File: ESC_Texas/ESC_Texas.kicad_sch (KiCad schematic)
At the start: 27 parts, among them IC2 nRF52840-QFAA-F-R7, J1 Conn_01x03_Pin, J2 Conn_01x10_Pin, J3 Conn_01x10_Pin, J4 Conn_01x05_Pin, J5 Conn_01x10_Pin, Y1 32MHz, Y2 32.768kHz

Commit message: Started PCB layouting
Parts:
- J4: footprint Connector_PinSocket_2.54mm:PinSocket_1x05_P2.54mm_Horizontal -> Connector_PinHeader_2.54mm:PinHeader_1x05_P2.54mm_Vertical
- J5: footprint Connector_PinSocket_2.54mm:PinSocket_1x10_P2.54mm_Vertical -> Connector_PinHeader_2.54mm:PinHeader_1x10_P2.54mm_Vertical
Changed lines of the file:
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@@
 	)
 	(no_connect
-		(at 49.53 45.72)
+		(at 48.26 45.72)
 	)
 	(no_connect
@@
 			)
 		)
-		(property "Footprint" "Connector_PinSocket_2.54mm:PinSocket_1x05_P2.54mm_Horizontal"
+		(property "Footprint" "Connector_PinHeader_2.54mm:PinHeader_1x05_P2.54mm_Vertical"
 			(at 158.75 125.73 0)
 			(effects
@@
 			)
 		)
-		(property "Footprint" "Connector_PinSocket_2.54mm:PinSocket_1x10_P2.54mm_Vertical"
+		(property "Footprint" "Connector_PinHeader_2.54mm:PinHeader_1x10_P2.54mm_Vertical"
 			(at 43.18 33.02 0)
 			(effects

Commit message: Layout done
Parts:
- removed C14: 1.2pF, Capacitor_SMD:C_0805_2012Metric, symbol Device:C
- removed J1: Conn_01x03_Pin, Connector_PinHeader_2.54mm:PinHeader_1x03_P2.54mm_Vertical, symbol Connector:Conn_01x03_Pin
- removed J3, J5: Conn_01x10_Pin, Connector_PinHeader_2.54mm:PinHeader_1x10_P2.54mm_Vertical, symbol Connector:Conn_01x10_Pin
- removed L3: 4.7nH, Inductor_SMD:L_1008_2520Metric_Pad1.43x2.20mm_HandSolder, symbol Device:L
- removed L4: 2.2nH, Inductor_SMD:L_1008_2520Metric_Pad1.43x2.20mm_HandSolder, symbol Device:L
- removed Y1: 32MHz, symbol Device:Crystal
- removed Y2: 32.768kHz, symbol Device:Crystal
- added J11: Conn_01x01_Pin, Connector_PinHeader_2.54mm:PinHeader_1x01_P2.54mm_Vertical, symbol Connector:Conn_01x01_Pin
- added J12, J2: Conn_01x05_Pin, Connector_PinHeader_2.54mm:PinHeader_1x05_P2.54mm_Vertical, symbol Connector:Conn_01x05_Pin
- added PS1: MP-K78U15-500R3L, MP-K78U15-500R3L:MPK78U15500R3L, symbol MP-K78U15-500R3L:MP-K78U15-500R3L
- added Y1: CM7V-T1A-32.768kHz, CM7V-T1A-32.768KHZ-12.5PF-20PPM-TA-QC:CM7V32768TBQA020, symbol CM7V-T1A-32.768KHZ-12.5PF-20PP:CM7V-T1A-32.768KHZ-12.5PF-20PPM-TA-QC
- added Y2: 32MHz, XRCGB32M000F2P29R0:XRCGB, symbol XRCGB32M000F2P29R0:XRCGB32M000F2P29R0
- renumbered C15 to C12, C12 to C13, C13 to C14, IC2 to IC1, J2 to J1
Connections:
- net ANT: no longer C11.2, IC1.32 (VSS_PA)
- net GND: now also PS1.2 (GND)
- net P0.02: now also J2.2 (Pin_2)
- net P0.13: now also J12.4 (Pin_4)
- net P0.28: now also J2.1 (Pin_1)
- net P1.00: now also J11.1 (Pin_1)
- net P1.14: now also J12.3 (Pin_3)
- net P1.15: now also J2.4 (Pin_4)
- net P1.17: now also J12.2 (Pin_2)
- net P1.18: now also J12.1 (Pin_1)
- net Po.03: now also J2.3 (Pin_3)
- net XC1: now also Y2.3 (XTAL_2)
- net XC2: now also Y2.1 (XTAL_1)
- net at C1.2, IC1.2 (P0.00/XL1): now also Y1.2
- net at C2.2, IC1.3 (P0.01/XL2): now also Y1.1
- new net +15V: PS1.3 (+VO)
- new net +36V: PS1.1 (VIN)
- new net VSS_PA: C11.2, IC1.32 (VSS_PA)
- no-connect marks 11 -> 7
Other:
- removed sheet Driver_subsheet_1
- added sheet Phase1 (Phase_subsheet.kicad_sch)
- added sheet Phase2 (Phase_subsheet.kicad_sch)
- added sheet Phase3 (Phase_subsheet.kicad_sch)
- moved on the sheet: C1, C10, C11, C12, C13, C14, C2, C3, C4, C5, C6, C7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

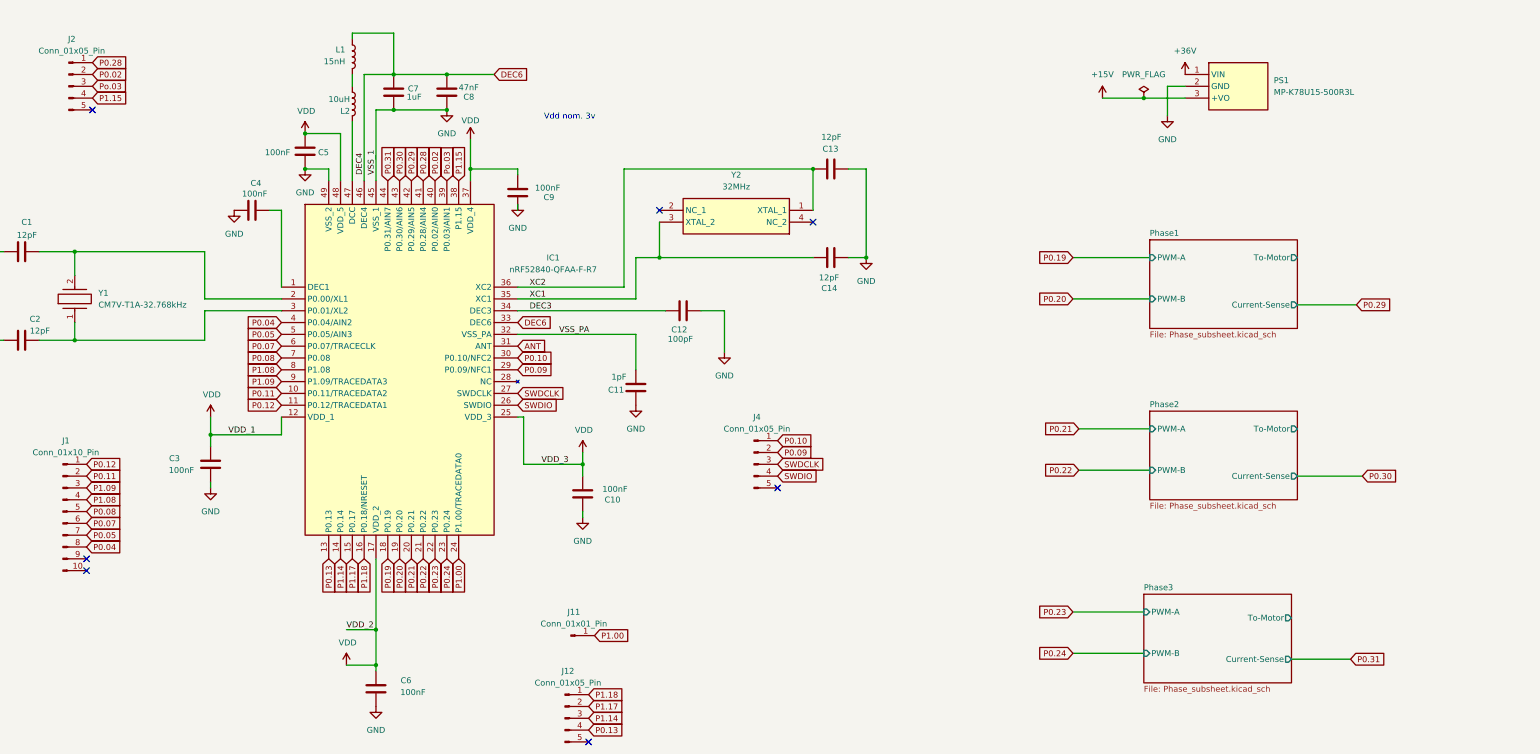
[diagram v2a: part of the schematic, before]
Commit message: Added bypass capacitors to dc/dc...
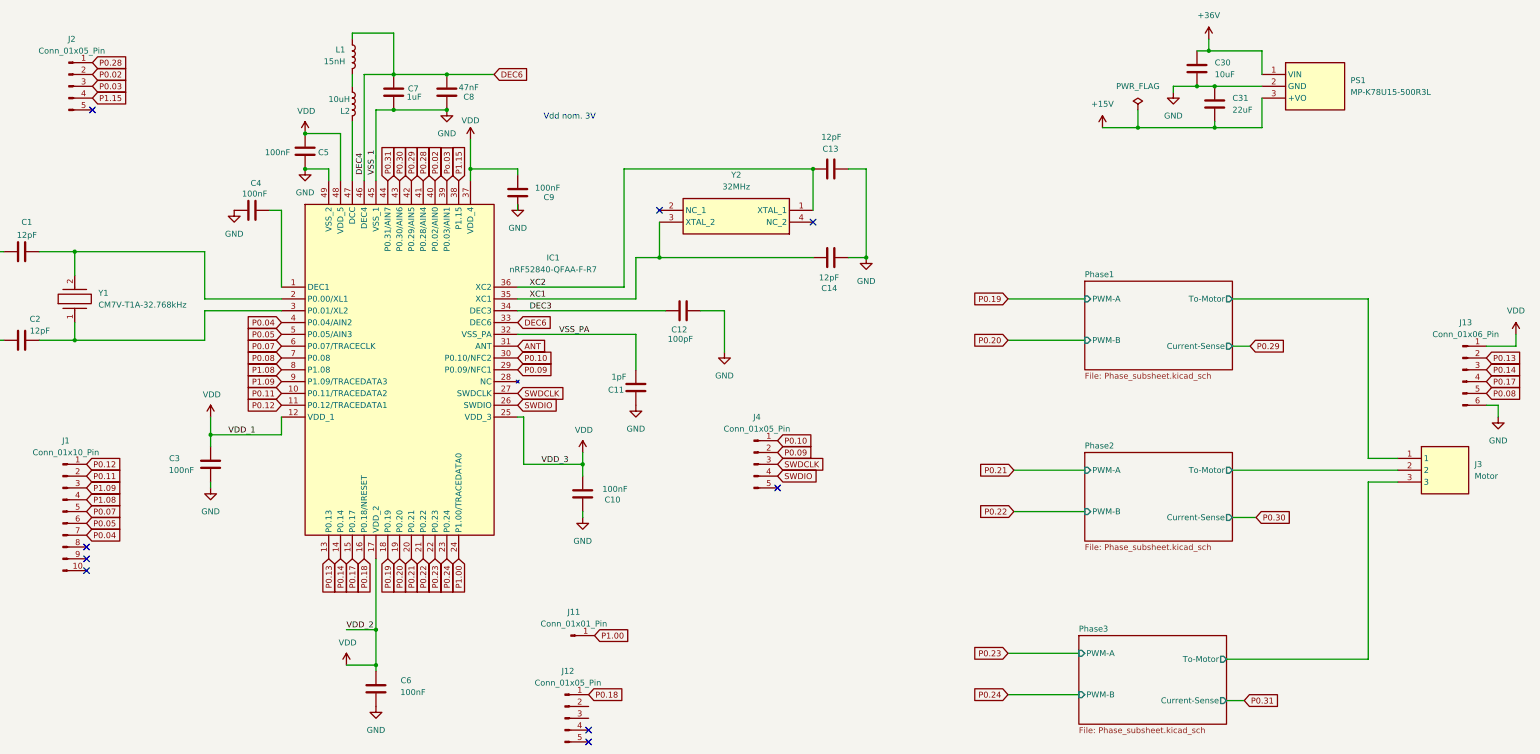
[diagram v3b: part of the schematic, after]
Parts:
- added C30: 10uF, symbol Device:C
- added C31: 22uF, symbol Device:C
- added J13: Conn_01x06_Pin, symbol Connector:Conn_01x06_Pin
- added J3: Motor, SHDRRA3W90P0X350_1X3_1110X920X691P, symbol 2350514-3:2350514-3
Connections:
- net +15V: now also C31.2
- net +36V: now also C30.1
- net GND: now also C30.2, C31.1, J13.6 (Pin_6)
- net P0.04: now also J1.7 (Pin_7); no longer J1.8 (Pin_8)
- net P0.05: now also J1.6 (Pin_6); no longer J1.7 (Pin_7)
- net P0.07: now also J1.5 (Pin_5); no longer J1.6 (Pin_6)
- net P0.08: now also J13.5 (Pin_5); no longer J1.5 (Pin_5)
- net P0.13: now also J13.2 (Pin_2); no longer J12.4 (Pin_4)
- net Phase1/To-Motor: now also J3.1
- net Phase2/To-Motor: now also J3.2
- net Phase3/To-Motor: now also J3.3
- net Po.03: no longer J2.3 (Pin_3)
- net VDD: now also J13.1 (Pin_1)
- net P1.14: no longer names the net of J12.3 (Pin_3)
- net P1.14: no longer IC1.14 (P0.14)
- net P1.17: no longer names the net of J12.2 (Pin_2)
- net P1.17: no longer IC1.15 (P0.17)
- net P1.18 renamed P0.18
- new net P0.03: J2.3 (Pin_3)
- new net P0.14: IC1.14 (P0.14), J13.3 (Pin_3)
- new net P0.17: IC1.15 (P0.17), J13.4 (Pin_4)
- no-connect marks 7 -> 9
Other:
- note added: "Vdd nom. 3V"
- note removed: "Vdd nom. 3v"
- moved on the sheet: PS1

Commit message: More routing done
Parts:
- removed J11: Conn_01x01_Pin, Connector_PinHeader_2.54mm:PinHeader_1x01_P2.54mm_Vertical, symbol Connector:Conn_01x01_Pin
- added C33, C34: 0.1uF, Capacitor_SMD:C_0805_2012Metric, symbol Device:C
- added IC11: LM3480IM3-3.3_NOPB, LM3480IM3-3.3_NOPB:SOT95P237X112-3N, symbol LM3480IM3-3_3_NOPB:LM3480IM3-3.3_NOPB
- C30, C31: footprint (none) -> Capacitor_SMD:C_0805_2012Metric
- J13: footprint (none) -> Connector_PinHeader_2.54mm:PinHeader_1x06_P2.54mm_Vertical
- J3: footprint SHDRRA3W90P0X350_1X3_1110X920X691P -> LIB_2350514-3:SHDRRA3W90P0X350_1X3_1110X920X691P
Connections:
- net +15V: now also C34.1, IC11.2 (IN)
- net GND: now also C33.2, C34.2, IC11.3 (GND)
- net P0.13: now also J13.4 (Pin_4); no longer J13.2 (Pin_2)
- net P0.17: now also J13.2 (Pin_2); no longer J13.4 (Pin_4)
- net P0.18: now also J12.2 (Pin_2); no longer J12.1 (Pin_1)
- net P1.00: now also J12.1 (Pin_1)
- net VDD: now also C33.1, IC11.1 (OUT)
- no-connect marks 9 -> 10
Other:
- moved on the sheet: C1, C10, C11, C12, C13, C14, C2, C3, C30, C31, C4, C5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

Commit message: PCB layout done
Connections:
- net Po.03 is gone; now on net P0.03: IC1.39 (P0.03/AIN1)
- net P0.02: now also J2.3 (Pin_3); no longer J2.2 (Pin_2)
- net P0.03: now also J2.4 (Pin_4); no longer J2.3 (Pin_3)
- net P0.28: now also J2.2 (Pin_2); no longer J2.1 (Pin_1)
- net P1.15: now also J2.5 (Pin_5); no longer J2.4 (Pin_4)

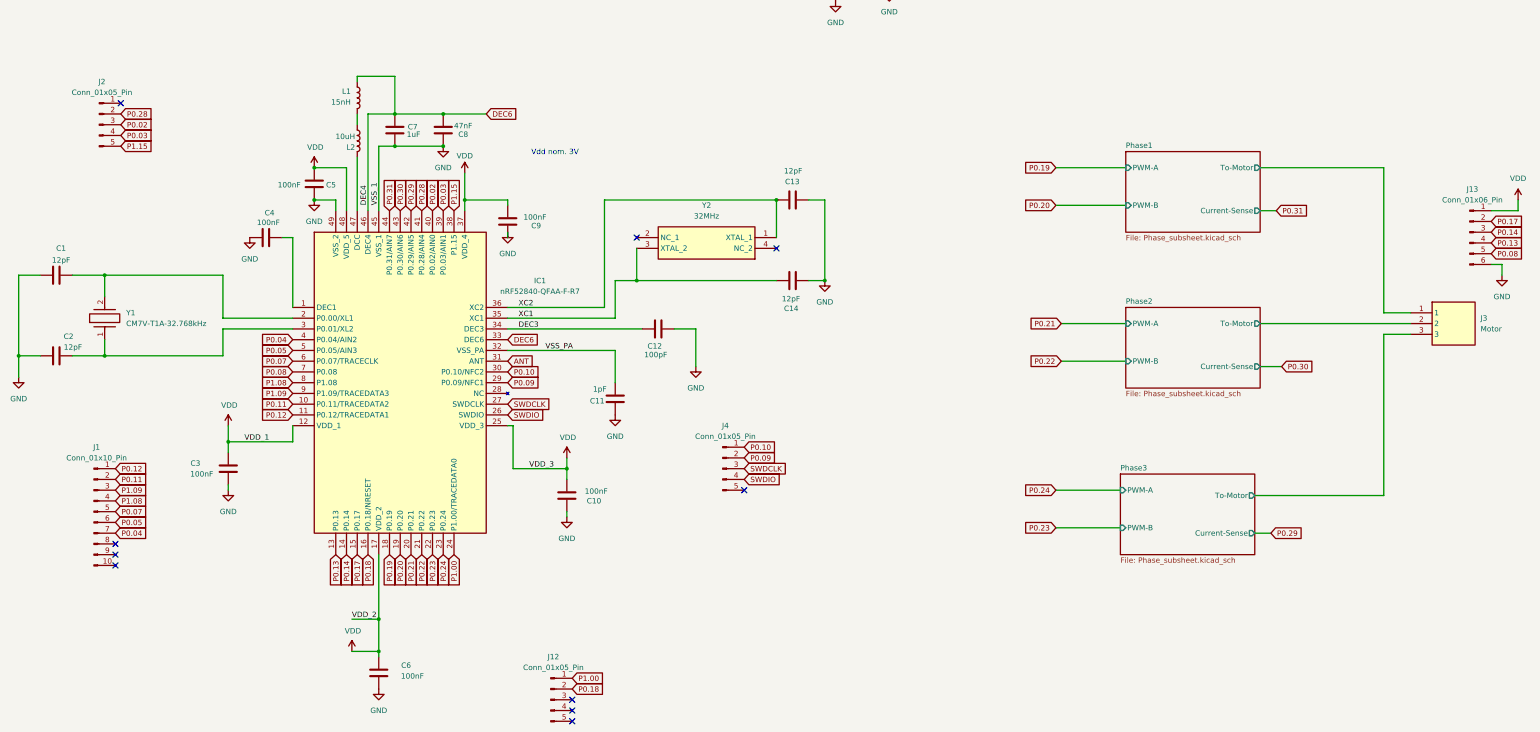
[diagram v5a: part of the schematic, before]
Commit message: Removed excess pin headers
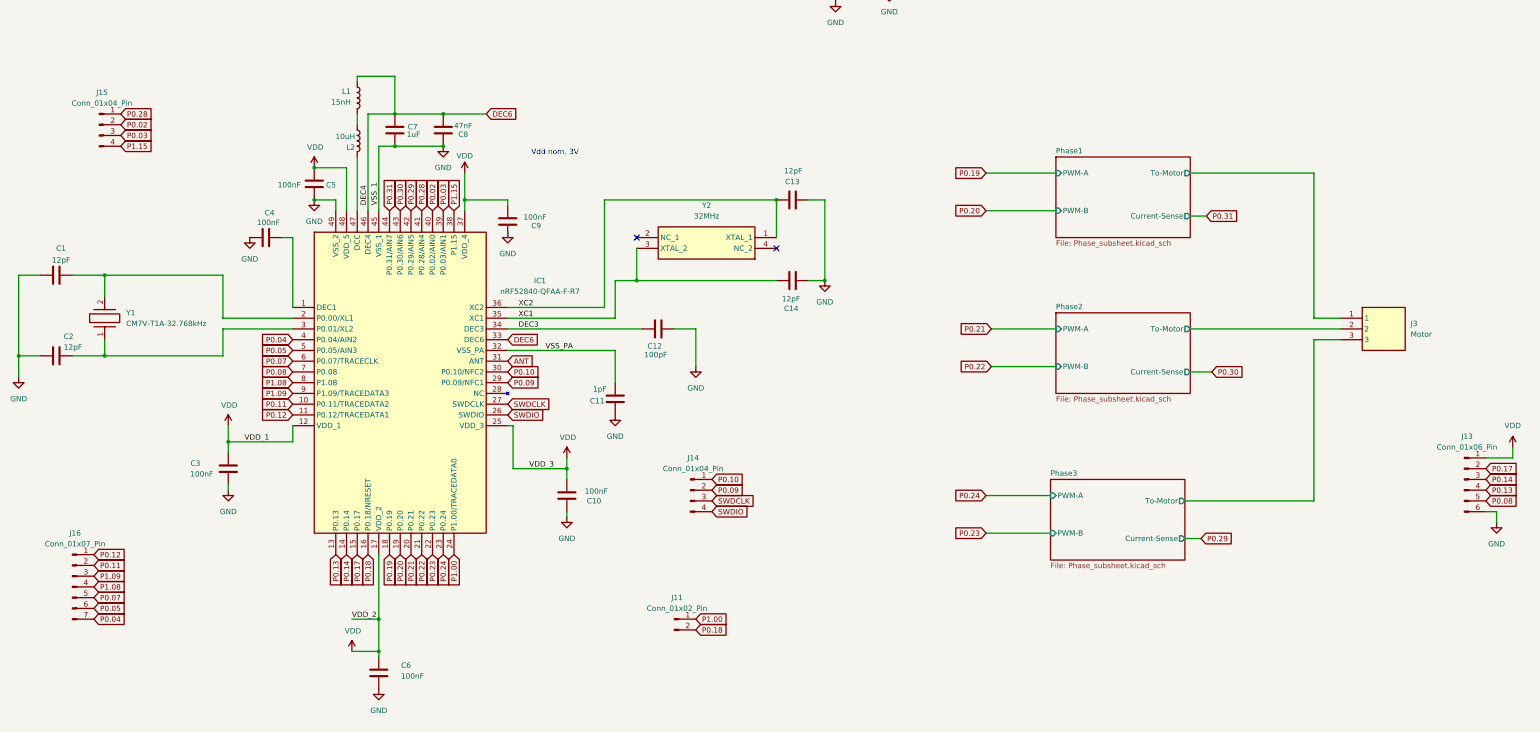
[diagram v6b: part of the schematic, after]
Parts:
- removed J1: Conn_01x10_Pin, Connector_PinHeader_2.54mm:PinHeader_1x10_P2.54mm_Vertical, symbol Connector:Conn_01x10_Pin
- removed J12, J2, J4: Conn_01x05_Pin, Connector_PinHeader_2.54mm:PinHeader_1x05_P2.54mm_Vertical, symbol Connector:Conn_01x05_Pin
- added J11: Conn_01x02_Pin, Connector_PinHeader_2.54mm:PinHeader_1x02_P2.54mm_Vertical, symbol Connector:Conn_01x02_Pin
- added J14, J15: Conn_01x04_Pin, Connector_PinHeader_2.54mm:PinHeader_1x04_P2.54mm_Vertical, symbol Connector:Conn_01x04_Pin
- added J16: Conn_01x07_Pin, Connector_PinHeader_2.54mm:PinHeader_1x07_P2.54mm_Vertical, symbol Connector:Conn_01x07_Pin
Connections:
- net P0.02: now also J15.2 (Pin_2)
- net P0.03: now also J15.3 (Pin_3)
- net P0.04: now also J16.7 (Pin_7)
- net P0.05: now also J16.6 (Pin_6)
- net P0.07: now also J16.5 (Pin_5)
- net P0.09: now also J14.2 (Pin_2)
- net P0.10: now also J14.1 (Pin_1)
- net P0.11: now also J16.2 (Pin_2)
- net P0.12: now also J16.1 (Pin_1)
- net P0.18: now also J11.2 (Pin_2)
- net P0.28: now also J15.1 (Pin_1)
- net P1.00: now also J11.1 (Pin_1)
- net P1.08: now also J16.4 (Pin_4)
- net P1.09: now also J16.3 (Pin_3)
- net P1.15: now also J15.4 (Pin_4)
- net SWDCLK: now also J14.3 (Pin_3)
- net SWDIO: now also J14.4 (Pin_4)
- no-connect marks 10 -> 2
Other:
- moved on the sheet: J13, J3

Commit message: More gnd vias added
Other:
- note added: "15 V regulator"
- note added: "3.3 V regulator"
- note added: "Input/Output to the motor"
- note added: "nRF52840 Circuit"
- moved on the sheet: C30, C31, C33, C34, IC11, J13, J3, PS1

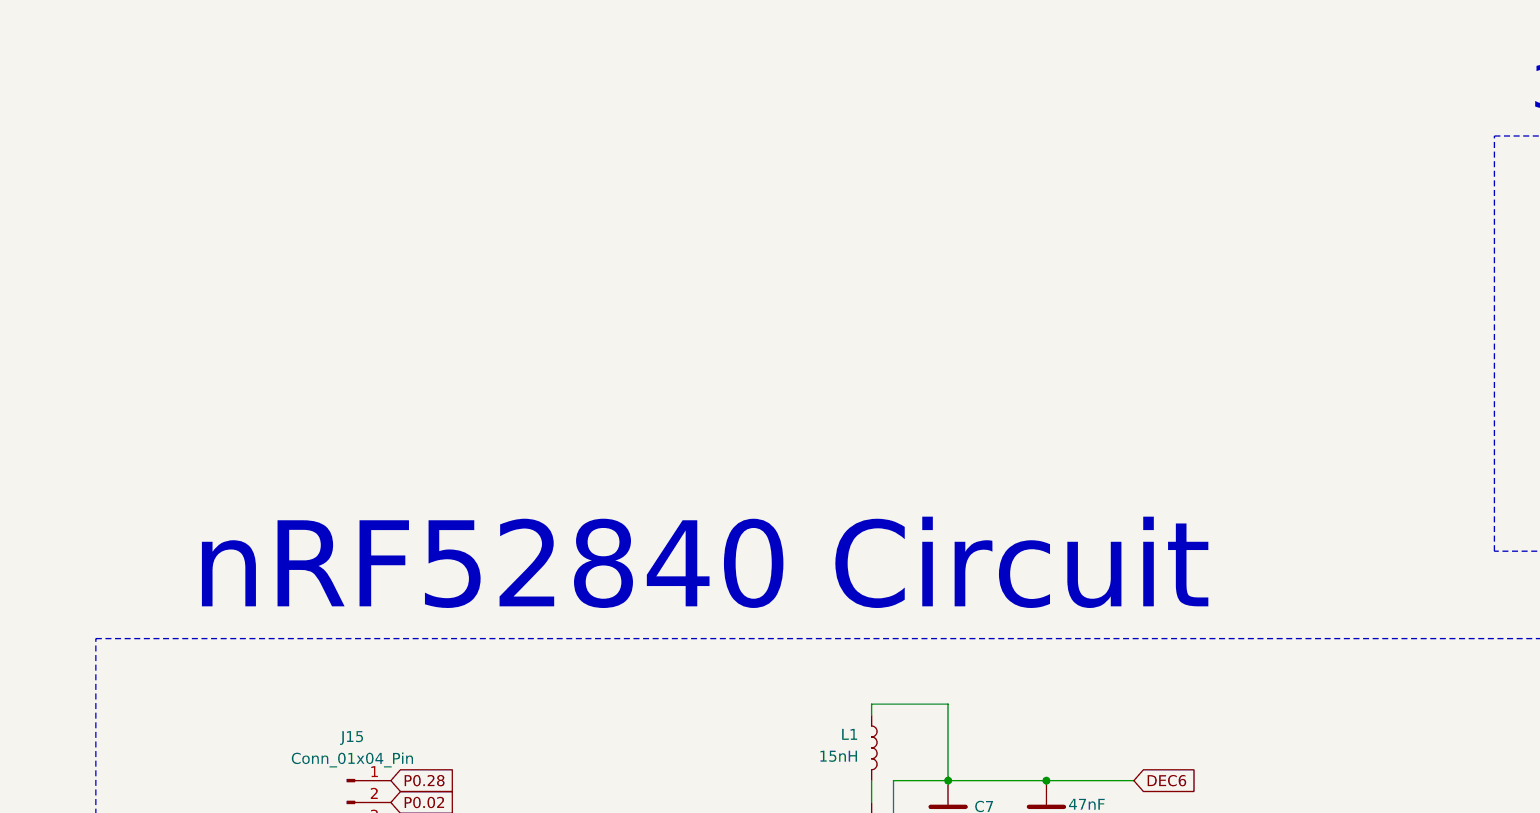
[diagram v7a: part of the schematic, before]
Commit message: Added capacitors and more
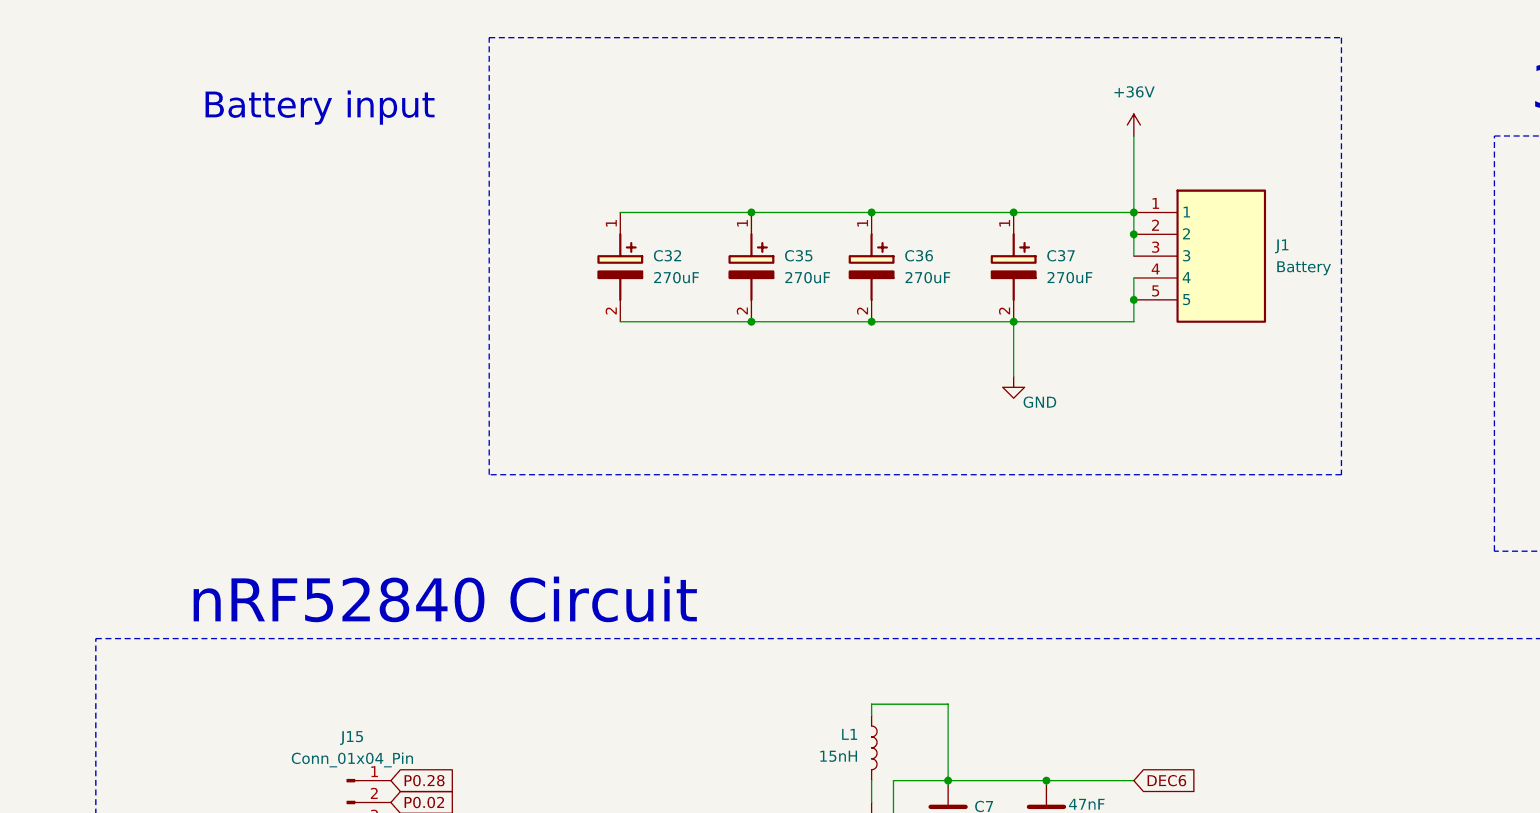
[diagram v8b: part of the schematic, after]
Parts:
- added C32, C35, C36, C37: 270uF, CAPPRD500W65D1000H1600, symbol A750MV277M1HAAE018:A750MV277M1HAAE018
- added J1: Battery, SHDRRA5W80P0X381_1X5_2024X920X720P, symbol 691322310005:691322310005
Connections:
- net +36V: now also C32.1 (+), C35.1 (+), C36.1 (+), C37.1 (+), J1.1, J1.2, J1.3
- net GND: now also C32.2 (-), C35.2 (-), C36.2 (-), C37.2 (-), J1.4, J1.5
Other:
- note added: "Battery input"
